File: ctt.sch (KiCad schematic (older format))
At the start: 7 parts, among them CN1 CONN_3, CN2 CONN_3

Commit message: 2011.05.19-i állapot.
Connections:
- net CTT/PS4/230V AC is gone; now on net CTT/PS4/230V AC: CN1.3 (P3)
- net CTT/PS4/230V AC: no longer CN1.1 (P1)
- new net CTT/PS4/230V AC: CN1.1 (P1)
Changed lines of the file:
@@
-EESchema Schematic File Version 2  date 2011.05.17. 21:59:39
+EESchema Schematic File Version 2  date 2011.05.19. 22:00:07
 LIBS:power
 LIBS:device
@@
 Sheet 1 10
 Title "CTT Transistor tester"
-Date "17 may 2011"
+Date "19 may 2011"
 Rev "1.0"
 Comp "Pozsar Zsolt"
@@
 Comment4 ""
 $EndDescr
+Text Notes 7700 6600 0    60   ~ 0
+CN2
+Text Notes 7900 6300 0    60   ~ 0
+CN3
+Text Notes 7600 4750 0    60   ~ 0
+CN2
+Text Notes 8200 5250 0    60   ~ 0
+CN1
+Text Notes 9450 5950 0    60   ~ 0
+CN2
+Text Notes 10100 4850 0    60   ~ 0
+CN1
 Connection ~ 8950 6600
 Wire Wire Line

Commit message: 2011.05.22-i állapot.
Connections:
- net CTT/PS4/230V AC is gone; now on net CTT/PS4/230V AC: CN1.3 (P3)
- net CTT/PS4/230V AC: no longer CN1.1 (P1)
- new net CTT/PS4/230V AC: CN1.1 (P1)

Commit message: 2011.05.22.esti állapot.
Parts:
- gave numbers to parts that had none: 5
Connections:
- net CTT/PS4/230V AC is gone; now on net 41: CN1.3 (P3)
- net 29: now also JC3.2
- net 30: now also JC4.2
- net 31: now also JC1.1, JC2.3
- net GND: now also JC1.3, JC2.1
- net 36ú renamed 36
- net 37ú renamed 37
- net CTT/PS1/+Um1 renamed 59
- net CTT/PS1/-Um1 renamed 58
- net CTT/PS1/POL renamed 33
- net CTT/PS2/+Um3 renamed 61
- net CTT/PS2/-Um3 renamed 60
- net CTT/PS3/+Um2 renamed 63
- net CTT/PS3/-Um2 renamed 62
- net CTT/PS4/230V AC renamed 39
- net CTT/PS4/PRT GND renamed 40

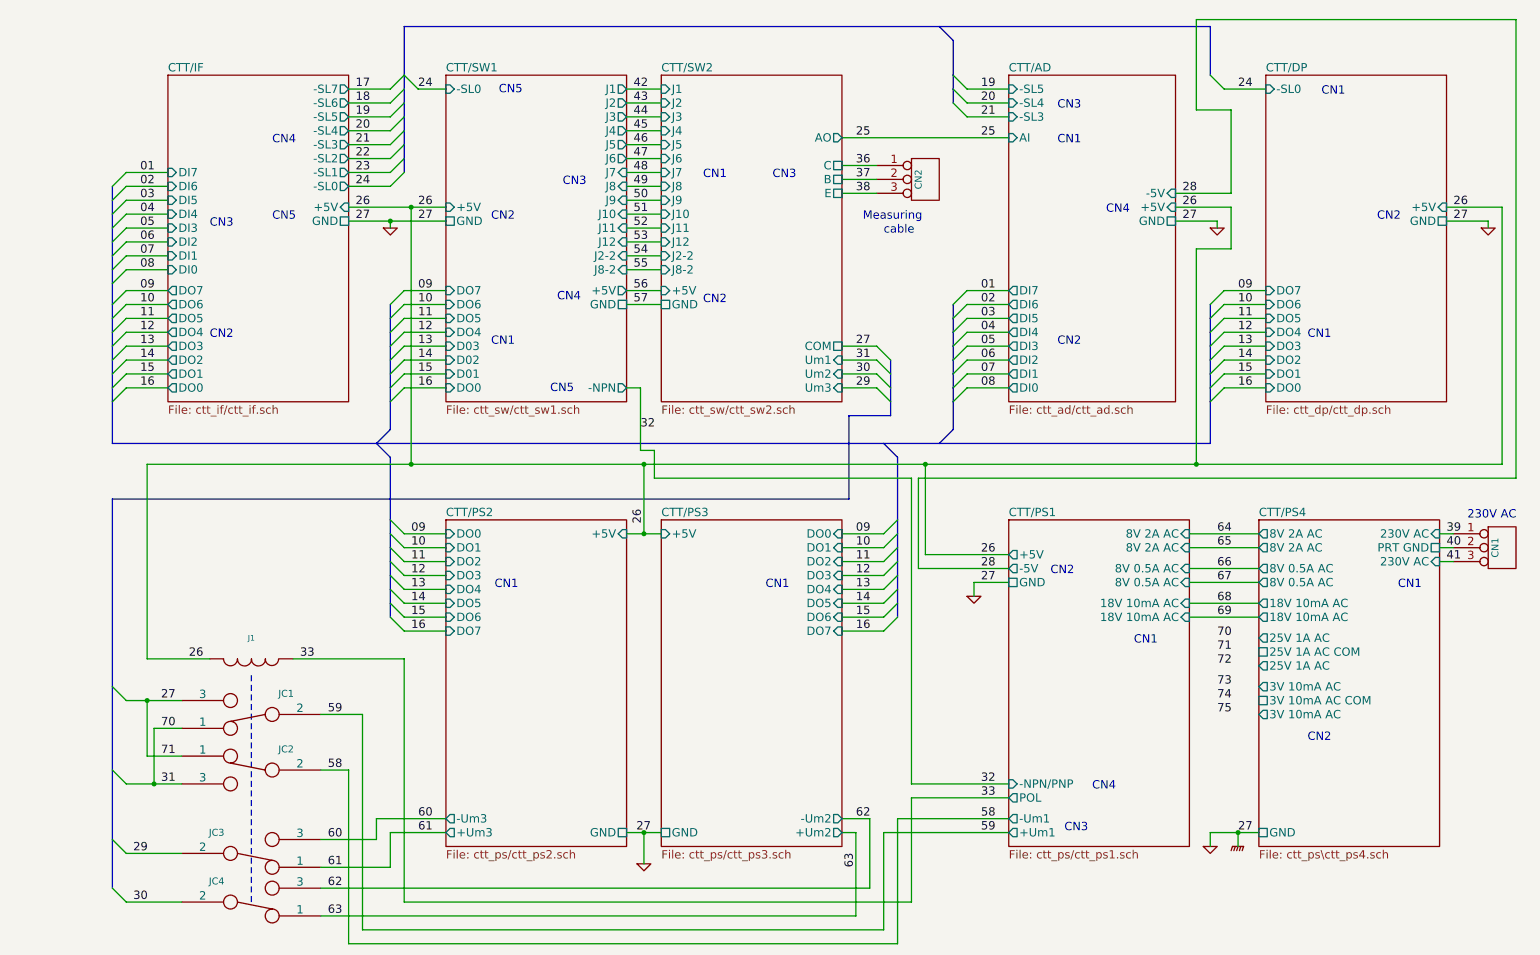
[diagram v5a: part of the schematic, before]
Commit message: 
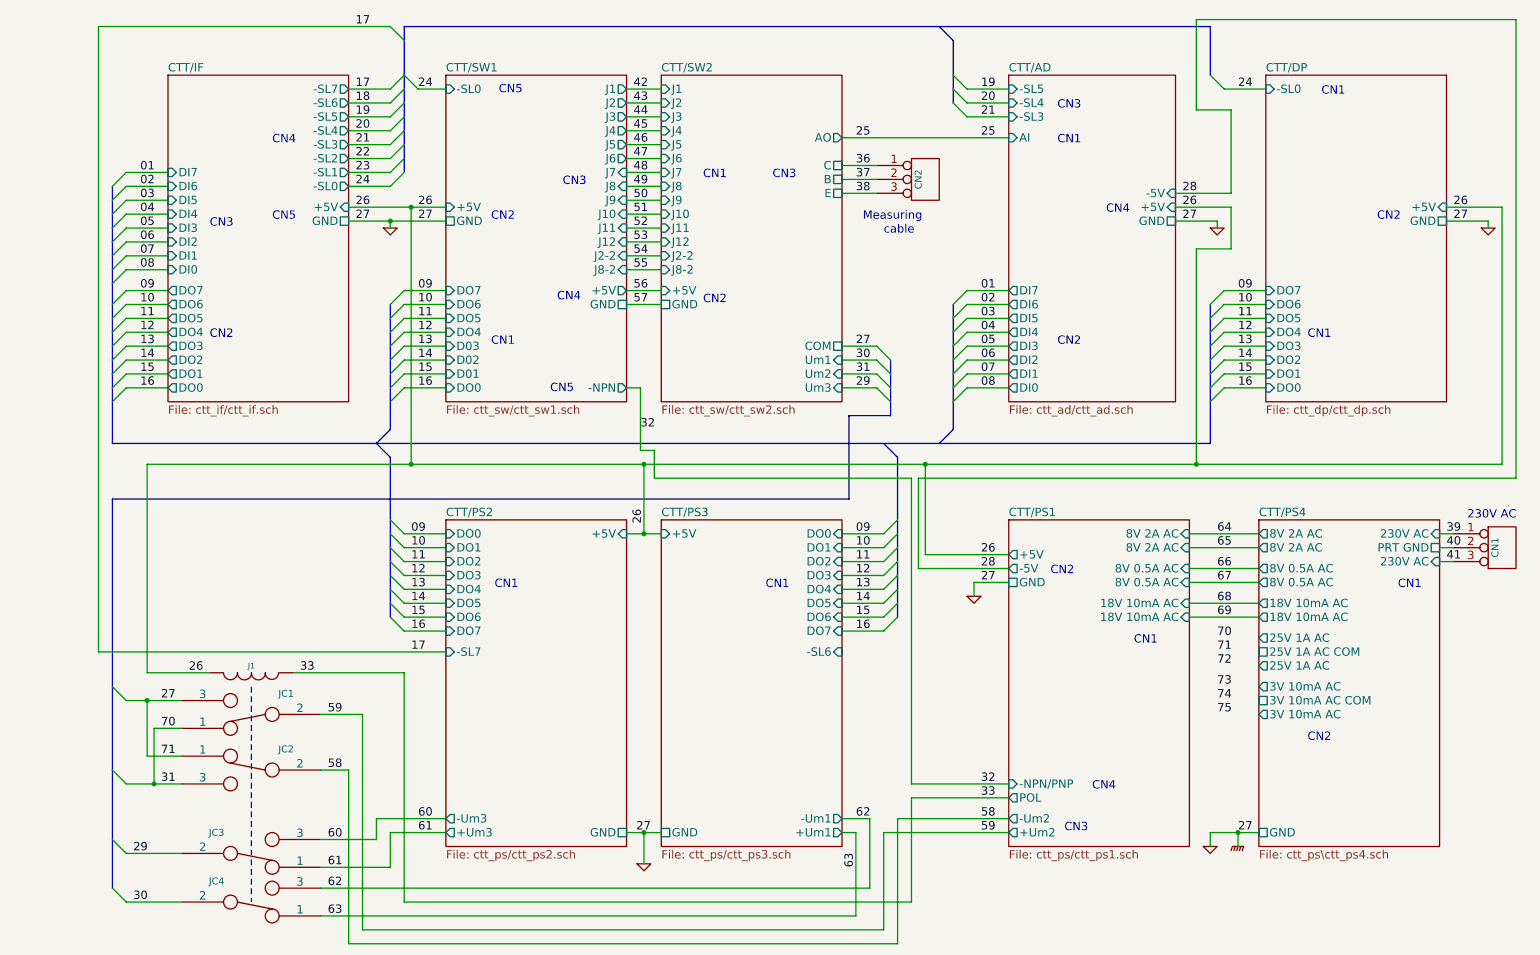
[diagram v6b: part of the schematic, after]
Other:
- moved on the sheet: J1
